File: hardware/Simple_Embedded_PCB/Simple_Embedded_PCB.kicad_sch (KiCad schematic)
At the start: 30 parts

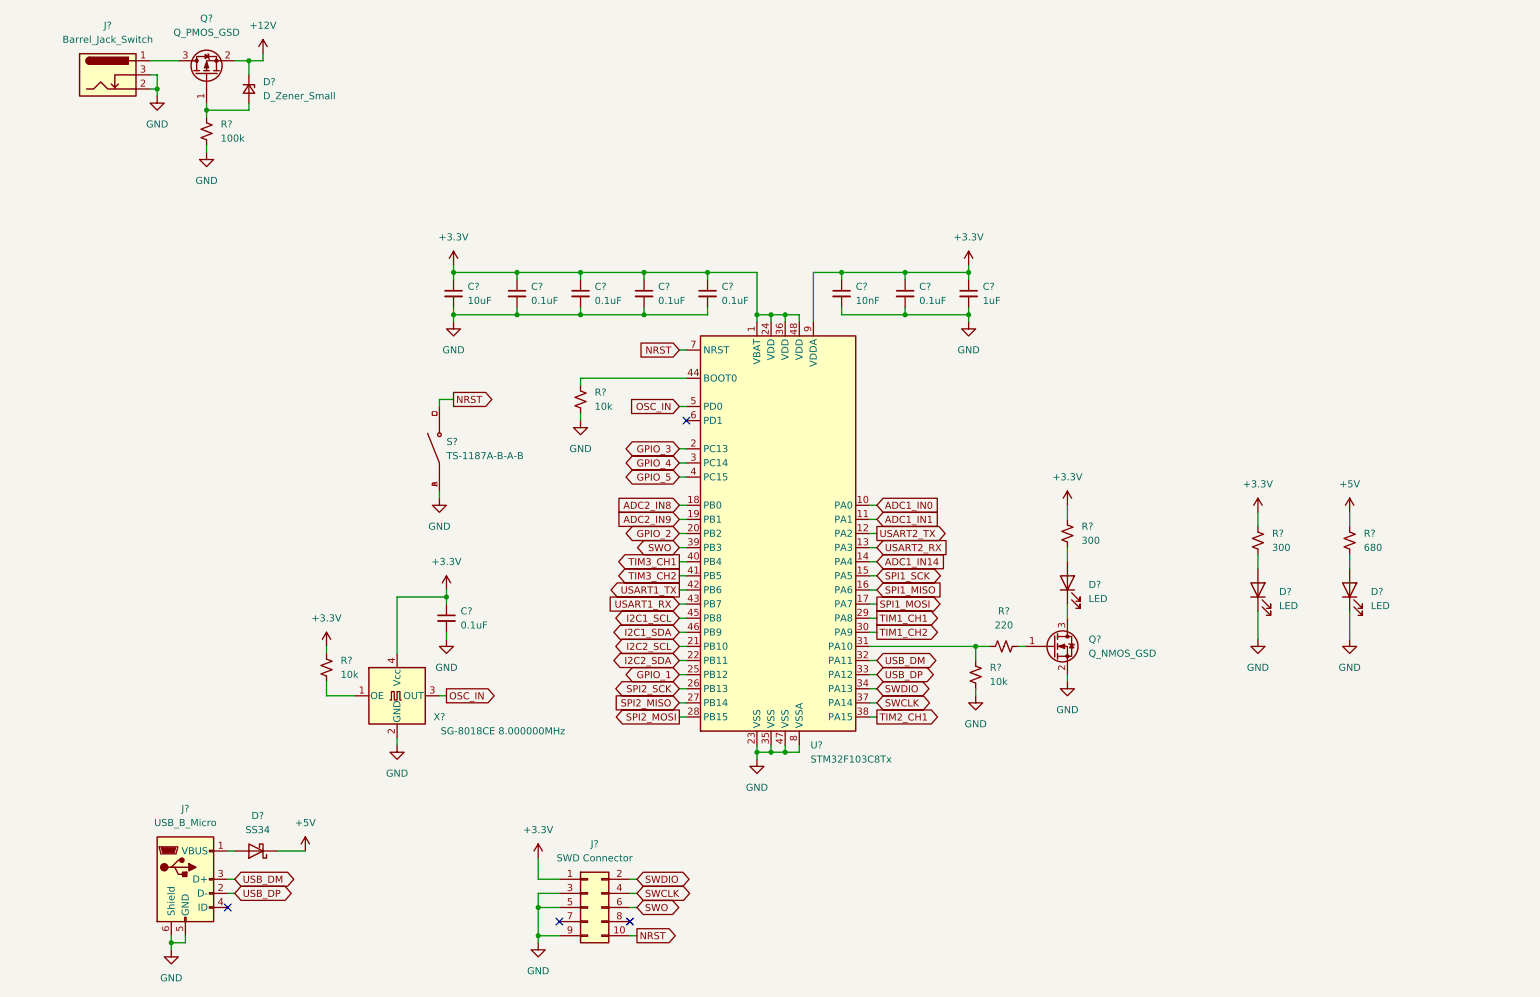
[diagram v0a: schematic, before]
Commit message: Update Simple_Embedded_PCB.kicad_sch
Added 5V and 3.3V regulators, add unpopulated header pins
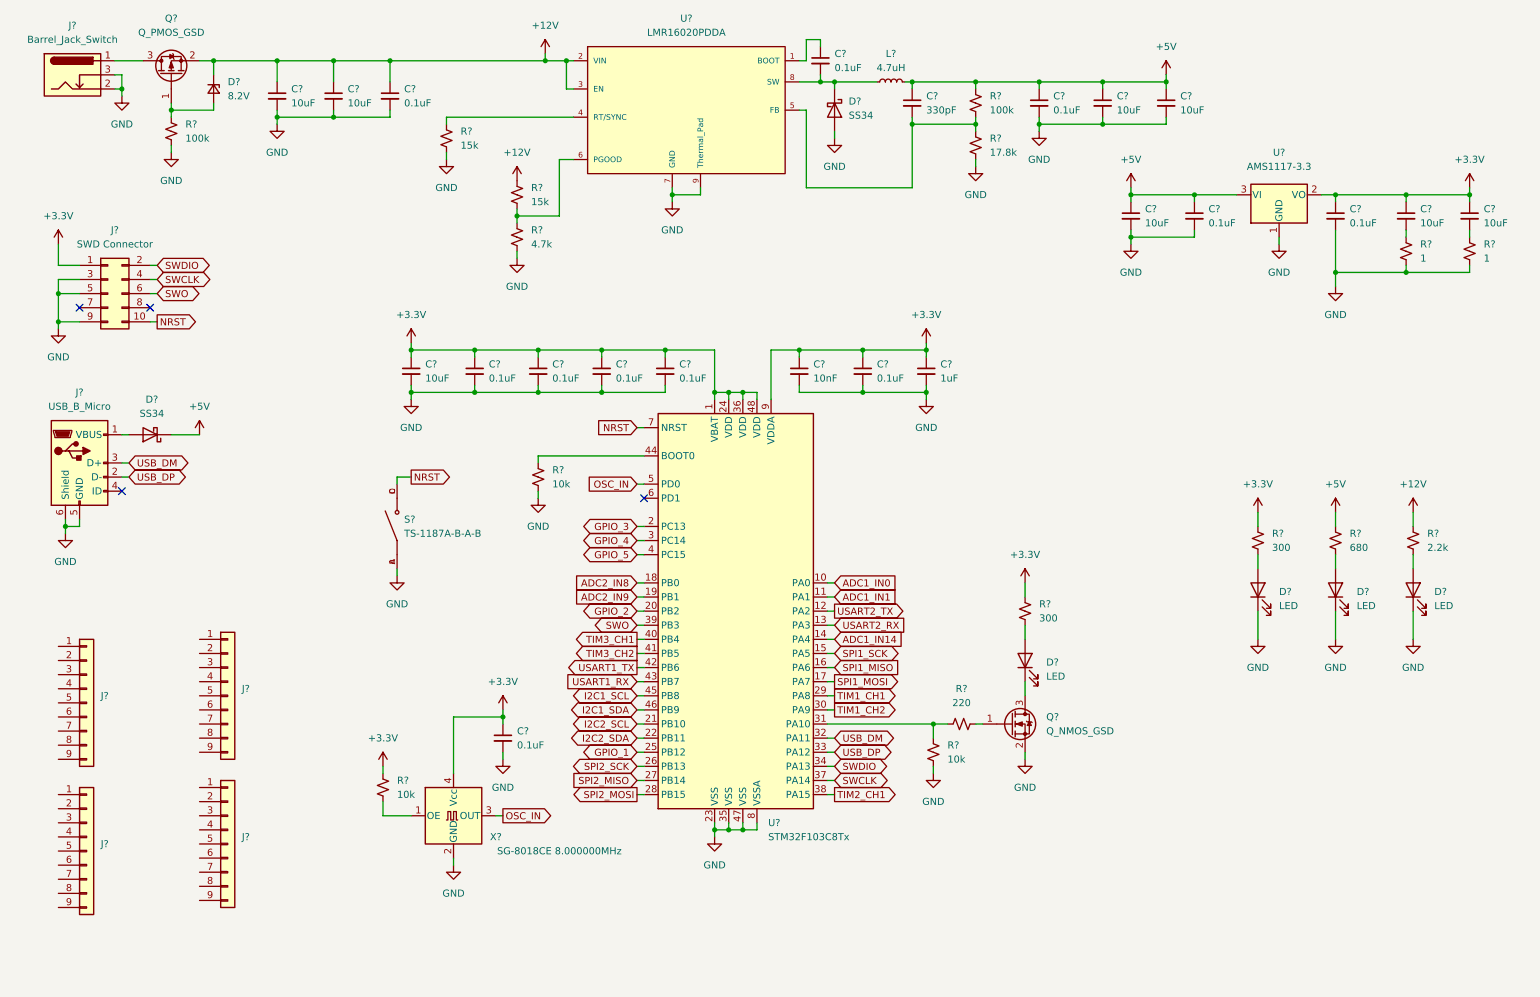
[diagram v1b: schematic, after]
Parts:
- added C? (x7): 10uF, symbol Device:C_Small
- added C? (x5): 0.1uF, symbol Device:C_Small
- added C?: 330pF, symbol Device:C_Small
- added D?: LED, LED_SMD:LED_0805_2012Metric, symbol Device:LED
- added D?: SS34, Diode_SMD:D_SMA, symbol Device:D_Schottky
- added J? (x4): Conn_01x09, Connector_PinHeader_2.54mm:PinHeader_1x09_P2.54mm_Vertical, symbol Connector_Generic:Conn_01x09
- added L?: 4.7uH, MySO:SUNLORD_SWPA6045S4R7MT, symbol Device:L_Small
- added R? (x2): 15k, symbol Device:R_Small_US
- added R?: 4.7k, symbol Device:R_Small_US
- added R?: 2.2k, symbol Device:R_Small_US
- added R? (x2): 1, symbol Device:R_Small_US
- added R?: 100k, symbol Device:R_Small_US
- added R?: 17.8k, symbol Device:R_Small_US
- added U?: LMR16020PDDA, MySO:8-PowerSOIC, symbol LMR16020PDDAR:LMR16020PDDA
- added U?: AMS1117-3.3, Package_TO_SOT_SMD:SOT-223-3_TabPin2, symbol Regulator_Linear:AMS1117-3.3
- D?: value D_Zener_Small -> 8.2V
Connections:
- net +12V: now also C?.1, C?.1, C?.1, R?.2, R?.2, U?.2 (VIN), U?.3 (EN)
- net +3.3V: now also C?.1, C?.1, C?.1, U?.2 (VO)
- net +5V: now also C?.1, C?.1, C?.1, C?.1, C?.1, C?.1, L?.2, R?.2, U?.3 (VI)
- net GND: now also C?.2, C?.2, C?.2, C?.2, C?.2, C?.2, C?.2, C?.2, C?.2, D?.1 (K), D?.2 (A), R?.1, R?.1, R?.1, R?.1, R?.1, U?.1 (GND), U?.7 (GND), U?.9 (Thermal_Pad)
- new net: C?.1, U?.1 (BOOT)
- new net: R?.2, U?.4 (RT/SYNC)
- new net: C?.2, R?.1, R?.2, U?.5 (FB)
- new net: R?.1, R?.2, U?.6 (PGOOD)
- new net: C?.2, D?.1 (K), L?.1, U?.8 (SW)
- new net: D?.2 (A), R?.1
- new net: C?.2, R?.2 (x2)
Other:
- moved on the sheet: C?, D?, J?, Q?, R?, S?, U?, X?

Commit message: Split MCU and Power into different sheets, created header pinouts, finished schematic and annotation
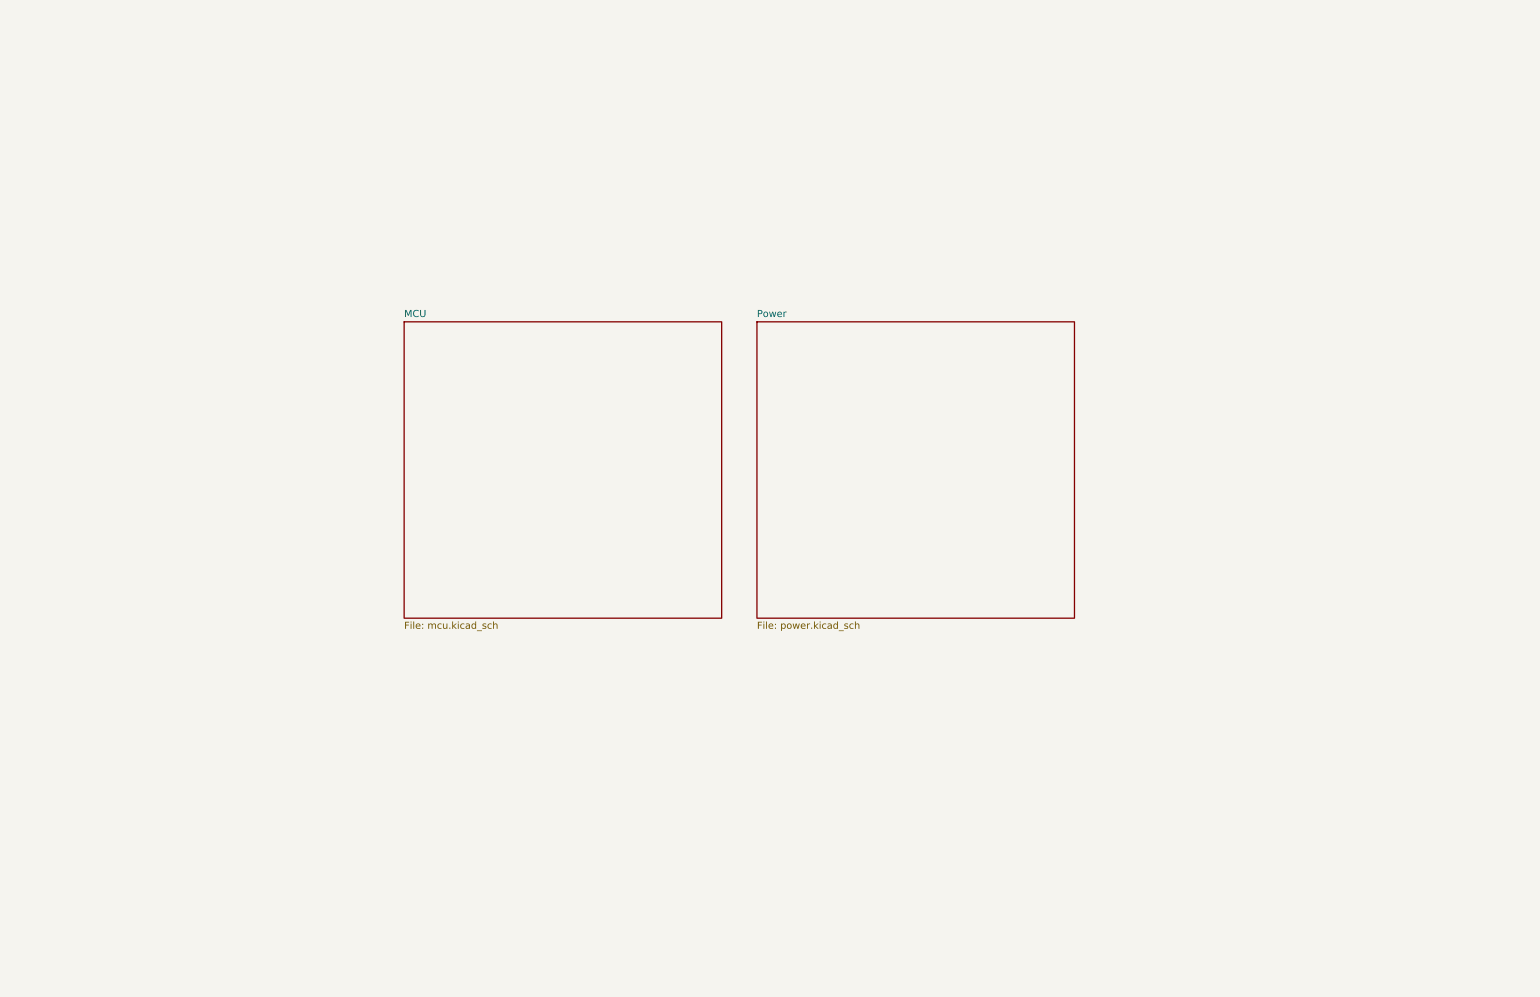
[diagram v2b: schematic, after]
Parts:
- removed C? (x8): 10uF, symbol Device:C_Small
- removed C? (x11): 0.1uF, symbol Device:C_Small
- removed C?: 330pF, symbol Device:C_Small
- removed C?: 1uF, symbol Device:C_Small
- removed C?: 10nF, symbol Device:C_Small
- removed D? (x4): LED, LED_SMD:LED_0805_2012Metric, symbol Device:LED
- removed D?: 8.2V, symbol Device:D_Zener_Small
- removed D? (x2): SS34, Diode_SMD:D_SMA, symbol Device:D_Schottky
- removed J?: SWD Connector, MySO:Amphenol-20021121-0-0-0, symbol Connector_Generic:Conn_02x05_Odd_Even
- removed J?: USB_B_Micro, Connector_USB:USB_Micro-B_Amphenol_10118194_Horizontal, symbol Connector:USB_B_Micro
- removed J? (x4): Conn_01x09, Connector_PinHeader_2.54mm:PinHeader_1x09_P2.54mm_Vertical, symbol Connector_Generic:Conn_01x09
- removed J?: Barrel_Jack_Switch, Connector_BarrelJack:BarrelJack_Horizontal, symbol Connector:Barrel_Jack_Switch
- removed L?: 4.7uH, MySO:SUNLORD_SWPA6045S4R7MT, symbol Device:L_Small
- removed Q?: Q_PMOS_GSD, Package_TO_SOT_SMD:SOT-23, symbol Device:Q_PMOS_GSD
- removed Q?: Q_NMOS_GSD, Package_TO_SOT_SMD:SOT-23, symbol Device:Q_NMOS_GSD
- removed R? (x2): 15k, symbol Device:R_Small_US
- removed R?: 4.7k, symbol Device:R_Small_US
- removed R? (x2): 100k, symbol Device:R_Small_US
- removed R? (x2): 300, symbol Device:R_Small_US
- removed R?: 2.2k, symbol Device:R_Small_US
- removed R? (x2): 1, symbol Device:R_Small_US
- removed R?: 680, symbol Device:R_Small_US
- removed R?: 220, symbol Device:R_Small_US
- removed R? (x3): 10k, symbol Device:R_Small_US
- removed R?: 17.8k, symbol Device:R_Small_US
- removed S?: TS-1187A-B-A-B, MySO:SW_TS-1187A-B-A-B, symbol TS-1187A-B-A-B:TS-1187A-B-A-B
- removed U?: LMR16020PDDA, MySO:8-PowerSOIC, symbol LMR16020PDDAR:LMR16020PDDA
- removed U?: AMS1117-3.3, Package_TO_SOT_SMD:SOT-223-3_TabPin2, symbol Regulator_Linear:AMS1117-3.3
- removed U?: STM32F103C8Tx, Package_QFP:LQFP-48_7x7mm_P0.5mm, symbol MCU_ST_STM32F1:STM32F103C8Tx
- removed X?: SG-8018CE 8.000000MHz, Oscillator:Oscillator_SMD_SeikoEpson_SG8002CE-4Pin_3.2x2.5mm, symbol Oscillator:SG-8002CE
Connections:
- no-connect marks 4 -> 0
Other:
- added sheet MCU (mcu.kicad_sch)
- added sheet Power (power.kicad_sch)

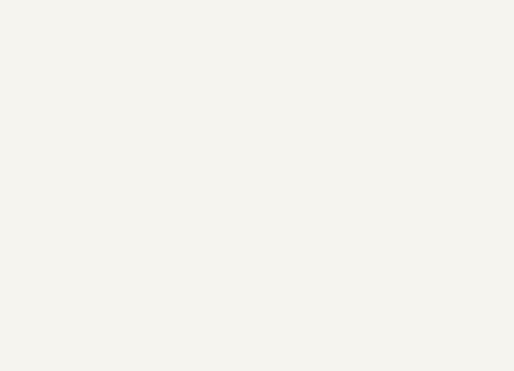
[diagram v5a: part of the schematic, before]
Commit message: Added tooling holes and put JLCPCB order number on back of board, added kicad_prl file to git ignore
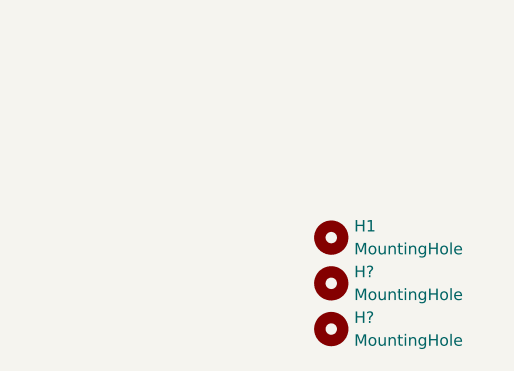
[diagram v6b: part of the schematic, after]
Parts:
- added H1, H? (x2): MountingHole, MySO:ToolingHole_JLCPCB, symbol Mechanical:MountingHole
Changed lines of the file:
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@@
     (comment 1 "Author: Austin Goergen")
+  )
+  (symbol (lib_id "Mechanical:MountingHole") (at 267.97 157.48 0) (unit 1)
+    (in_bom yes) (on_board yes) (fields_autoplaced)
+    (property "Reference" "H?" (id 0) (at 270.51 156.2099 0)
+      (effects (font (size 1.27 1.27)) (justify left))
+    )
+    (property "Value" "MountingHole" (id 1) (at 270.51 158.7499 0)
+      (effects (font (size 1.27 1.27)) (justify left))
+    )
+    (property "Footprint" "MySO:ToolingHole_JLCPCB" (id 2) (at 267.97 157.48 0)
+      (effects (font (size 1.27 1.27)) hide)
+    )
+    (property "Datasheet" "~" (id 3) (at 267.97 157.48 0)
+      (effects (font (size 1.27 1.27)) hide)
+    )
+  )
+  (symbol (lib_id "Mechanical:MountingHole") (at 267.97 152.4 0) (unit 1)
+    (in_bom yes) (on_board yes) (fields_autoplaced)
+    (property "Reference" "H1" (id 0) (at 270.51 151.1299 0)
+      (effects (font (size 1.27 1.27)) (justify left))
+    )
+    (property "Value" "MountingHole" (id 1) (at 270.51 153.6699 0)
+      (effects (font (size 1.27 1.27)) (justify left))
+    )
+    (property "Footprint" "MySO:ToolingHole_JLCPCB" (id 2) (at 267.97 152.4 0)
+      (effects (font (size 1.27 1.27)) hide)
+    )
+    (property "Datasheet" "~" (id 3) (at 267.97 152.4 0)
+      (effects (font (size 1.27 1.27)) hide)
+    )
+  )
+  (symbol (lib_id "Mechanical:MountingHole") (at 267.97 162.56 0) (unit 1)
+    (in_bom yes) (on_board yes) (fields_autoplaced)
+    (property "Reference" "H?" (id 0) (at 270.51 161.2899 0)
+      (effects (font (size 1.27 1.27)) (justify left))
+    )
+    (property "Value" "MountingHole" (id 1) (at 270.51 163.8299 0)
+      (effects (font (size 1.27 1.27)) (justify left))
+    )
+    (property "Footprint" "MySO:ToolingHole_JLCPCB" (id 2) (at 267.97 162.56 0)
+      (effects (font (size 1.27 1.27)) hide)
+    )
+    (property "Datasheet" "~" (id 3) (at 267.97 162.56 0)
+      (effects (font (size 1.27 1.27)) hide)
+    )
   )
   (sheet (at 147.32 69.85) (size 57.15 53.34) (fields_autoplaced)
@@
       (reference "D7") (unit 1) (value "SS34") (footprint "Diode_SMD:D_SMA")
     )
+    (path "/2d52195a-901a-4e0b-9e79-ff221f8eb32f"
+      (reference "H1") (unit 1) (value "MountingHole") (footprint "MySO:ToolingHole_JLCPCB")
+    )
+    (path "/251e4cb3-db00-4ec3-a34f-8b668e19d569"
+      (reference "H?") (unit 1) (value "MountingHole") (footprint "MySO:ToolingHole_JLCPCB")
+    )
+    (path "/6419c0ec-89d6-4989-85fa-2ef10b705c33"
+      (reference "H?") (unit 1) (value "MountingHole") (footprint "MySO:ToolingHole_JLCPCB")
+    )
     (path "/ae79c7b9-f7a9-43ca-b7bc-1b2649a48113/c5a8047f-af7b-4f40-b928-c92943f394a4"

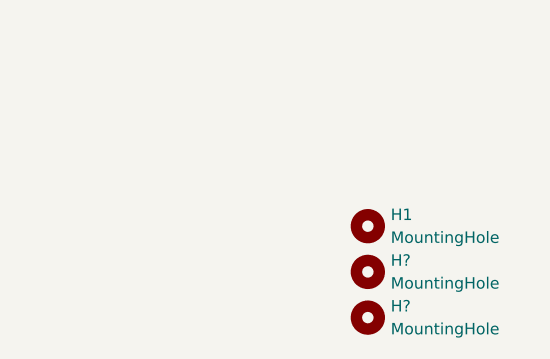
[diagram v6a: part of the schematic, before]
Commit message: Added JLCPCB part numbers
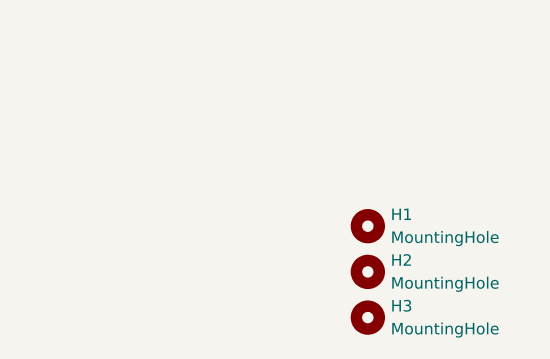
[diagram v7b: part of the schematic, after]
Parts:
- gave numbers to parts that had none: 2
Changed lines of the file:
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@@
   (symbol (lib_id "Mechanical:MountingHole") (at 267.97 157.48 0) (unit 1)
     (in_bom yes) (on_board yes) (fields_autoplaced)
-    (property "Reference" "H?" (id 0) (at 270.51 156.2099 0)
+    (property "Reference" "H2" (id 0) (at 270.51 156.2099 0)
       (effects (font (size 1.27 1.27)) (justify left))
     )
@@
   (symbol (lib_id "Mechanical:MountingHole") (at 267.97 162.56 0) (unit 1)
     (in_bom yes) (on_board yes) (fields_autoplaced)
-    (property "Reference" "H?" (id 0) (at 270.51 161.2899 0)
+    (property "Reference" "H3" (id 0) (at 270.51 161.2899 0)
       (effects (font (size 1.27 1.27)) (justify left))
     )
@@
     )
     (path "/251e4cb3-db00-4ec3-a34f-8b668e19d569"
-      (reference "H?") (unit 1) (value "MountingHole") (footprint "MySO:ToolingHole_JLCPCB")
+      (reference "H2") (unit 1) (value "MountingHole") (footprint "MySO:ToolingHole_JLCPCB")
     )
     (path "/6419c0ec-89d6-4989-85fa-2ef10b705c33"
-      (reference "H?") (unit 1) (value "MountingHole") (footprint "MySO:ToolingHole_JLCPCB")
+      (reference "H3") (unit 1) (value "MountingHole") (footprint "MySO:ToolingHole_JLCPCB")
     )
     (path "/ae79c7b9-f7a9-43ca-b7bc-1b2649a48113/c5a8047f-af7b-4f40-b928-c92943f394a4"

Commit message: Changed KiCad project to use symbols, footprints, and 3D models from project itself.
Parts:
- H1, H2, H3: footprint MySO:ToolingHole_JLCPCB -> Simple_Embedded_PCB:ToolingHole_JLCPCB
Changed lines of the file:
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@@
       (effects (font (size 1.27 1.27)) (justify left))
     )
-    (property "Footprint" "MySO:ToolingHole_JLCPCB" (id 2) (at 267.97 157.48 0)
+    (property "Footprint" "Simple_Embedded_PCB:ToolingHole_JLCPCB" (id 2) (at 267.97 157.48 0)
       (effects (font (size 1.27 1.27)) hide)
     )
@@
       (effects (font (size 1.27 1.27)) (justify left))
     )
-    (property "Footprint" "MySO:ToolingHole_JLCPCB" (id 2) (at 267.97 152.4 0)
+    (property "Footprint" "Simple_Embedded_PCB:ToolingHole_JLCPCB" (id 2) (at 267.97 152.4 0)
       (effects (font (size 1.27 1.27)) hide)
     )
@@
       (effects (font (size 1.27 1.27)) (justify left))
     )
-    (property "Footprint" "MySO:ToolingHole_JLCPCB" (id 2) (at 267.97 162.56 0)
+    (property "Footprint" "Simple_Embedded_PCB:ToolingHole_JLCPCB" (id 2) (at 267.97 162.56 0)
       (effects (font (size 1.27 1.27)) hide)
     )
@@
     )
     (path "/2d52195a-901a-4e0b-9e79-ff221f8eb32f"
-      (reference "H1") (unit 1) (value "MountingHole") (footprint "MySO:ToolingHole_JLCPCB")
+      (reference "H1") (unit 1) (value "MountingHole") (footprint "Simple_Embedded_PCB:ToolingHole_JLCPCB")
     )
     (path "/251e4cb3-db00-4ec3-a34f-8b668e19d569"
-      (reference "H2") (unit 1) (value "MountingHole") (footprint "MySO:ToolingHole_JLCPCB")
+      (reference "H2") (unit 1) (value "MountingHole") (footprint "Simple_Embedded_PCB:ToolingHole_JLCPCB")
     )
     (path "/6419c0ec-89d6-4989-85fa-2ef10b705c33"
-      (reference "H3") (unit 1) (value "MountingHole") (footprint "MySO:ToolingHole_JLCPCB")
+      (reference "H3") (unit 1) (value "MountingHole") (footprint "Simple_Embedded_PCB:ToolingHole_JLCPCB")
     )
     (path "/ae79c7b9-f7a9-43ca-b7bc-1b2649a48113/c5a8047f-af7b-4f40-b928-c92943f394a4"
@@
     )
     (path "/ae79c7b9-f7a9-43ca-b7bc-1b2649a48113/cb318a72-e149-40b8-837f-b3318ca06223"
-      (reference "J2") (unit 1) (value "SWD Connector") (footprint "MySO:Amphenol-20021121-0-0-0")
+      (reference "J2") (unit 1) (value "SWD Connector") (footprint "Simple_Embedded_PCB:Amphenol-20021121-0-0-0")
     )
     (path "/ae79c7b9-f7a9-43ca-b7bc-1b2649a48113/4388cfac-9858-4550-bcf8-7b9773d01a84"
@@
     )
     (path "/162250f7-d927-4da0-b1ba-5afd7e082fc5/97ff25a2-47d5-41e2-b087-6dbded30eaf2"
-      (reference "L1") (unit 1) (value "4.7uH") (footprint "MySO:SUNLORD_SWPA6045S4R7MT")
+      (reference "L1") (unit 1) (value "4.7uH") (footprint "Simple_Embedded_PCB:SUNLORD_SWPA6045S4R7MT")
     )
     (path "/ae79c7b9-f7a9-43ca-b7bc-1b2649a48113/807ad40f-591c-4019-8343-f20234d91c3d"
@@
     )
     (path "/ae79c7b9-f7a9-43ca-b7bc-1b2649a48113/dc50db42-2c8e-43c5-a279-42a88593f19a"
-      (reference "S1") (unit 1) (value "TS-1187A-B-A-B") (footprint "MySO:SW_TS-1187A-B-A-B")
+      (reference "S1") (unit 1) (value "TS-1187A-B-A-B") (footprint "Simple_Embedded_PCB:SW_TS-1187A-B-A-B")
     )
     (path "/ae79c7b9-f7a9-43ca-b7bc-1b2649a48113/152fafeb-31de-48f6-94d1-2da7f481a430"
@@
     )
     (path "/162250f7-d927-4da0-b1ba-5afd7e082fc5/80a7e5ef-2327-4700-b5a8-37d90514b621"
-      (reference "U2") (unit 1) (value "LMR16020PDDA") (footprint "MySO:8-PowerSOIC")
+      (reference "U2") (unit 1) (value "LMR16020PDDA") (footprint "Simple_Embedded_PCB:8-PowerSOIC")
     )
     (path "/162250f7-d927-4da0-b1ba-5afd7e082fc5/b07efc5e-573b-4c23-a7d1-4177b82fe425"
